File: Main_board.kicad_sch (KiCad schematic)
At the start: 199 parts, among them J1 USB_C_Receptacle_USB2.0_14P, J2 Conn_02x03_Odd_Even, SW1 SW_Push, SW10 SW_Push, SW11 SW_Push, SW12 SW_Push, SW13 SW_Push, SW14 SW_Push, SW15 SW_Push, SW16 SW_Push, SW17 SW_Push, SW18 SW_Push, SW19 SW_Push, SW2 SW_Push, SW20 SW_Push, SW21 SW_Push, SW22 SW_Push, SW23 SW_Push, SW24 SW_Push, SW25 SW_Push, SW26 SW_Push, SW27 SW_Push, SW28 SW_Push, SW29 SW_Push, SW3 SW_Push, SW30 SW_Push, SW31 SW_Push, SW32 SW_Push, SW33 SW_Push, SW34 SW_Push, SW35 SW_Push, SW36 SW_Push, SW37 SW_Push, SW38 SW_Push, SW39 SW_Push, SW4 SW_Push, SW40 SW_Push, SW41 SW_Push, SW42 SW_Push, SW43 SW_Push, SW44 SW_Push, SW45 SW_Push, SW46 SW_Push, SW47 SW_Push, SW48 SW_Push, SW49 SW_Push, SW5 SW_Push, SW50 SW_Push, SW51 SW_Push, SW52 SW_Push, SW53 SW_Push, SW54 SW_Push, SW55 SW_Push, SW56 SW_Push, SW57 SW_Push, SW58 SW_Push, SW59 SW_Push, SW6 SW_Push, SW60 SW_Push, SW61 SW_Push, SW62 SW_Push, SW63 SW_Push, SW64 SW_Push, SW65 SW_Push, SW66 SW_Push, SW67 SW_Push, SW68 SW_Push, SW69 SW_Push, SW7 SW_Push, SW70 SW_Push, SW71 SW_Push, SW72 SW_Push, SW73 SW_Push, SW74 SW_Push, SW75 SW_Push, SW76 SW_Push, SW77 SW_Push, SW78 SW_Push, SW79 SW_Push, SW8 SW_Push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

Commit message: Finished the main board's design
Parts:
- added D104, D105, D106, D107, D108, D109, D110, D111, D112, D113, D114, D115, D116, D117, D118, D119, D120, D121, D122, D123, D124, D125, D126, D127, D128, D129, D130, D131, D132, D133, D134, D135, D136, D137, D138, D139, D140, D141, D142, D143, D144, D145, D146, D147, D148, D149, D150, D151, D152, D153, D154, D155, D156, D157, D158, D159, D160, D161, D162, D163, D164, D165, D166, D167, D168, D169, D170, D171, D172, D173, D174, D175, D176, D177, D178, D179, D180, D181, D182, D183, D184, D185: SK6805, LED_SMD:LED_SK6805_PLCC4_2.4x2.7mm_P1.3mm, symbol LED:SK6805
- added H1, H2, H3, H4: MountingHole, MountingHole:MountingHole_2.2mm_M2, symbol Mechanical:MountingHole
- added U11: MT3608_Module, Footprints:MT3608-Module, symbol Custom Symbols:MT3608_Module
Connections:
- net GND: now also D104.2 (VSS), D105.2 (VSS), D106.2 (VSS), D107.2 (VSS), D108.2 (VSS), D109.2 (VSS), D110.2 (VSS), D111.2 (VSS), D112.2 (VSS), D113.2 (VSS), D114.2 (VSS), D115.2 (VSS), D116.2 (VSS), D117.2 (VSS), D118.2 (VSS), D119.2 (VSS), D120.2 (VSS), D121.2 (VSS), D122.2 (VSS), D123.2 (VSS), D124.2 (VSS), D125.2 (VSS), D126.2 (VSS), D127.2 (VSS), D128.2 (VSS), D129.2 (VSS), D130.2 (VSS), D131.2 (VSS), D132.2 (VSS), D133.2 (VSS), D134.2 (VSS), D135.2 (VSS), D136.2 (VSS), D137.2 (VSS), D138.2 (VSS), D139.2 (VSS), D140.2 (VSS), D141.2 (VSS), D142.2 (VSS), D143.2 (VSS), D144.2 (VSS), D145.2 (VSS), D146.2 (VSS), D147.2 (VSS), D148.2 (VSS), D149.2 (VSS), D150.2 (VSS), D151.2 (VSS), D152.2 (VSS), D153.2 (VSS), D154.2 (VSS), D155.2 (VSS), D156.2 (VSS), D157.2 (VSS), D158.2 (VSS), D159.2 (VSS), D160.2 (VSS), D161.2 (VSS), D162.2 (VSS), D163.2 (VSS), D164.2 (VSS), D165.2 (VSS), D166.2 (VSS), D167.2 (VSS), D168.2 (VSS), D169.2 (VSS), D170.2 (VSS), D171.2 (VSS), D172.2 (VSS), D173.2 (VSS), D174.2 (VSS), D175.2 (VSS), D176.2 (VSS), D177.2 (VSS), D178.2 (VSS), D179.2 (VSS), D180.2 (VSS), D181.2 (VSS), D182.2 (VSS), D183.2 (VSS), D184.2 (VSS), D185.2 (VSS), U11.2 (VIN-), U11.4 (VOUT-)
- net M3V3: now also C2.1, U3.30 (VDDH), U3.32 (VBUS), U11.1 (VIN+)
- net MBT_PIN: now also U3.11 (P0.02)
- net MFLT: now also U3.7 (P1.14); no longer U3.24 (P0.08)
- net MID1: now also U3.25 (P1.08); no longer U3.61 (P1.01)
- net MID2: now also U3.20 (P0.04)
- net MID3: now also U3.24 (P0.08); no longer U3.60 (P1.03)
- net MID4: now also U3.27 (P0.11); no longer U3.56 (P1.04)
- net MINT1: now also U3.23 (P0.07); no longer U3.59 (P1.05)
- net MINT2: now also U3.18 (P0.01); no longer U3.57 (P1.06)
- net MINT3: now also U3.26 (P1.09); no longer U3.58 (P1.07)
- net MINT4: now also U3.22 (P0.06); no longer U3.25 (P1.08)
- net MRESET: now also U3.5 (P1.12)
- net MSCL: now also U3.19 (P0.26)
- net MSDA: now also U3.21 (P0.05); no longer U3.26 (P1.09)
- net MUSB_DET: now also U3.3 (P1.10)
- net MVB_EN: now also U3.13 (P0.28); no longer U3.22 (P0.06)
- net VDD: now also D104.4 (VDD), D105.4 (VDD), D106.4 (VDD), D107.4 (VDD), D108.4 (VDD), D109.4 (VDD), D110.4 (VDD), D111.4 (VDD), D112.4 (VDD), D113.4 (VDD), D114.4 (VDD), D115.4 (VDD), D116.4 (VDD), D117.4 (VDD), D118.4 (VDD), D119.4 (VDD), D120.4 (VDD), D121.4 (VDD), D122.4 (VDD), D123.4 (VDD), D124.4 (VDD), D125.4 (VDD), D126.4 (VDD), D127.4 (VDD), D128.4 (VDD), D129.4 (VDD), D130.4 (VDD), D131.4 (VDD), D132.4 (VDD), D133.4 (VDD), D134.4 (VDD), D135.4 (VDD), D136.4 (VDD), D137.4 (VDD), D138.4 (VDD), D139.4 (VDD), D140.4 (VDD), D141.4 (VDD), D142.4 (VDD), D143.4 (VDD), D144.4 (VDD), D145.4 (VDD), D146.4 (VDD), D147.4 (VDD), D148.4 (VDD), D149.4 (VDD), D150.4 (VDD), D151.4 (VDD), D152.4 (VDD), D153.4 (VDD), D154.4 (VDD), D155.4 (VDD), D156.4 (VDD), D157.4 (VDD), D158.4 (VDD), D159.4 (VDD), D160.4 (VDD), D161.4 (VDD), D162.4 (VDD), D163.4 (VDD), D164.4 (VDD), D165.4 (VDD), D166.4 (VDD), D167.4 (VDD), D168.4 (VDD), D169.4 (VDD), D170.4 (VDD), D171.4 (VDD), D172.4 (VDD), D173.4 (VDD), D174.4 (VDD), D175.4 (VDD), D176.4 (VDD), D177.4 (VDD), D178.4 (VDD), D179.4 (VDD), D180.4 (VDD), D181.4 (VDD), D182.4 (VDD), D183.4 (VDD), D184.4 (VDD), D185.4 (VDD), U11.3 (VOUT+); no longer C2.1, C7.1, J1.A4 (VBUS), J1.A9 (VBUS), J1.B4 (VBUS), J1.B9 (VBUS), R12.2, U2.1 (VBUS), U2.8 (VBUS), U3.30 (VDDH), U3.32 (VBUS), U5.4 (V_{DD})
- net MVBUS_SW renamed MV_SW
- new net: D168.1 (DOUT), D169.3 (DIN)
- new net: D167.1 (DOUT), D168.3 (DIN)
- new net: D165.1 (DOUT), D166.3 (DIN)
- new net: D164.1 (DOUT), D165.3 (DIN)
- new net: D142.1 (DOUT), D143.3 (DIN)
- new net: D141.1 (DOUT), D142.3 (DIN)
- new net: D138.1 (DOUT), D139.3 (DIN)
- new net: D137.1 (DOUT), D138.3 (DIN)
- new net: D153.3 (DIN), D154.1 (DOUT)
- new net: D154.3 (DIN), D155.1 (DOUT)
- new net: D112.1 (DOUT), D113.3 (DIN)
- new net: D111.1 (DOUT), D112.3 (DIN)
- new net: D180.3 (DIN), D181.1 (DOUT)
- new net: D181.3 (DIN), D182.1 (DOUT)
- new net: D131.3 (DIN), D132.1 (DOUT)
- new net: D117.1 (DOUT), D132.3 (DIN)
- new net: D130.3 (DIN), D131.1 (DOUT)
- new net: D127.3 (DIN), D128.1 (DOUT)
- new net: D128.3 (DIN), D129.1 (DOUT)
- new net: D105.1 (DOUT), D106.3 (DIN)
- new net: D104.1 (DOUT), D105.3 (DIN)
- new net: D120.3 (DIN), D121.1 (DOUT)
- new net: D121.3 (DIN), D122.1 (DOUT)
- new net: D177.3 (DIN), D178.1 (DOUT)
- new net: D178.3 (DIN), D179.1 (DOUT)
- new net: D139.1 (DOUT), D140.3 (DIN)
- new net: D172.1 (DOUT), D173.3 (DIN)
- new net: D171.1 (DOUT), D172.3 (DIN)
- new net: D143.1 (DOUT), D144.3 (DIN)
- new net: D118.3 (DIN), D119.1 (DOUT)
- new net: D119.3 (DIN), D120.1 (DOUT)
- new net: D151.3 (DIN), D152.1 (DOUT)
- new net: D152.3 (DIN), D153.1 (DOUT)
- new net: D115.1 (DOUT), D116.3 (DIN)
- new net: D114.1 (DOUT), D115.3 (DIN)
- new net: D106.1 (DOUT), D107.3 (DIN)
- new net: D134.1 (DOUT), D135.3 (DIN)
- new net: D133.1 (DOUT), D134.3 (DIN)
- new net: D150.3 (DIN), D151.1 (DOUT)
- new net: D116.1 (DOUT), D117.3 (DIN)
- new net: D184.3 (DIN), D185.1 (DOUT)
- new net: D174.1 (DOUT), D185.3 (DIN)
- new net: D166.1 (DOUT), D167.3 (DIN)
- new net: D129.3 (DIN), D130.1 (DOUT)
- new net: D122.3 (DIN), D123.1 (DOUT)
- new net: D118.1 (DOUT), D133.3 (DIN)
- new net: D147.1 (DOUT), D161.3 (DIN)
- new net: D146.1 (DOUT), D147.3 (DIN)
- new net: D162.1 (DOUT), D163.3 (DIN)
- new net: D148.1 (DOUT), D162.3 (DIN)
- new net: D173.1 (DOUT), D174.3 (DIN)
- new net: D183.3 (DIN), D184.1 (DOUT)
- new net: D109.1 (DOUT), D110.3 (DIN)
- new net: D108.1 (DOUT), D109.3 (DIN)
- new net: D155.3 (DIN), D156.1 (DOUT)
- new net: D156.3 (DIN), D157.1 (DOUT)
- new net: D163.1 (DOUT), D164.3 (DIN)
- new net: D157.3 (DIN), D158.1 (DOUT)
- new net: D158.3 (DIN), D159.1 (DOUT)
- new net: D140.1 (DOUT), D141.3 (DIN)
- new net: D148.3 (DIN), D149.1 (DOUT)
- new net: D136.1 (DOUT), D137.3 (DIN)
- new net: D135.1 (DOUT), D136.3 (DIN)
- new net: D107.1 (DOUT), D108.3 (DIN)
- new net: D110.1 (DOUT), D111.3 (DIN)
- new net: D113.1 (DOUT), D114.3 (DIN)
- new net: D182.3 (DIN), D183.1 (DOUT)
- new net: D179.3 (DIN), D180.1 (DOUT)
- new net: D149.3 (DIN), D150.1 (DOUT)
- new net: D145.1 (DOUT), D146.3 (DIN)
- new net: D175.3 (DIN), D176.1 (DOUT)
- new net: D176.3 (DIN), D177.1 (DOUT)
- new net: D170.1 (DOUT), D171.3 (DIN)
- new net: D123.3 (DIN), D124.1 (DOUT)
- new net: D124.3 (DIN), D125.1 (DOUT)
- new net: D169.1 (DOUT), D170.3 (DIN)
- new net: D126.3 (DIN), D127.1 (DOUT)
- new net: D144.1 (DOUT), D145.3 (DIN)
- new net: D160.3 (DIN), D161.1 (DOUT)
- new net: D125.3 (DIN), D126.1 (DOUT)
- new net: D159.3 (DIN), D160.1 (DOUT)
- new net MLEDs: D104.3 (DIN), U3.56 (P1.04)
- new net MVBUS: C7.1, J1.A4 (VBUS), J1.A9 (VBUS), J1.B4 (VBUS), J1.B9 (VBUS), R12.2, U2.1 (VBUS), U2.8 (VBUS), U5.4 (V_{DD})
- no-connect marks 14 -> 18
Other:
- moved on the sheet: C1, C2, D83, R10, R5, R8, R9, U3

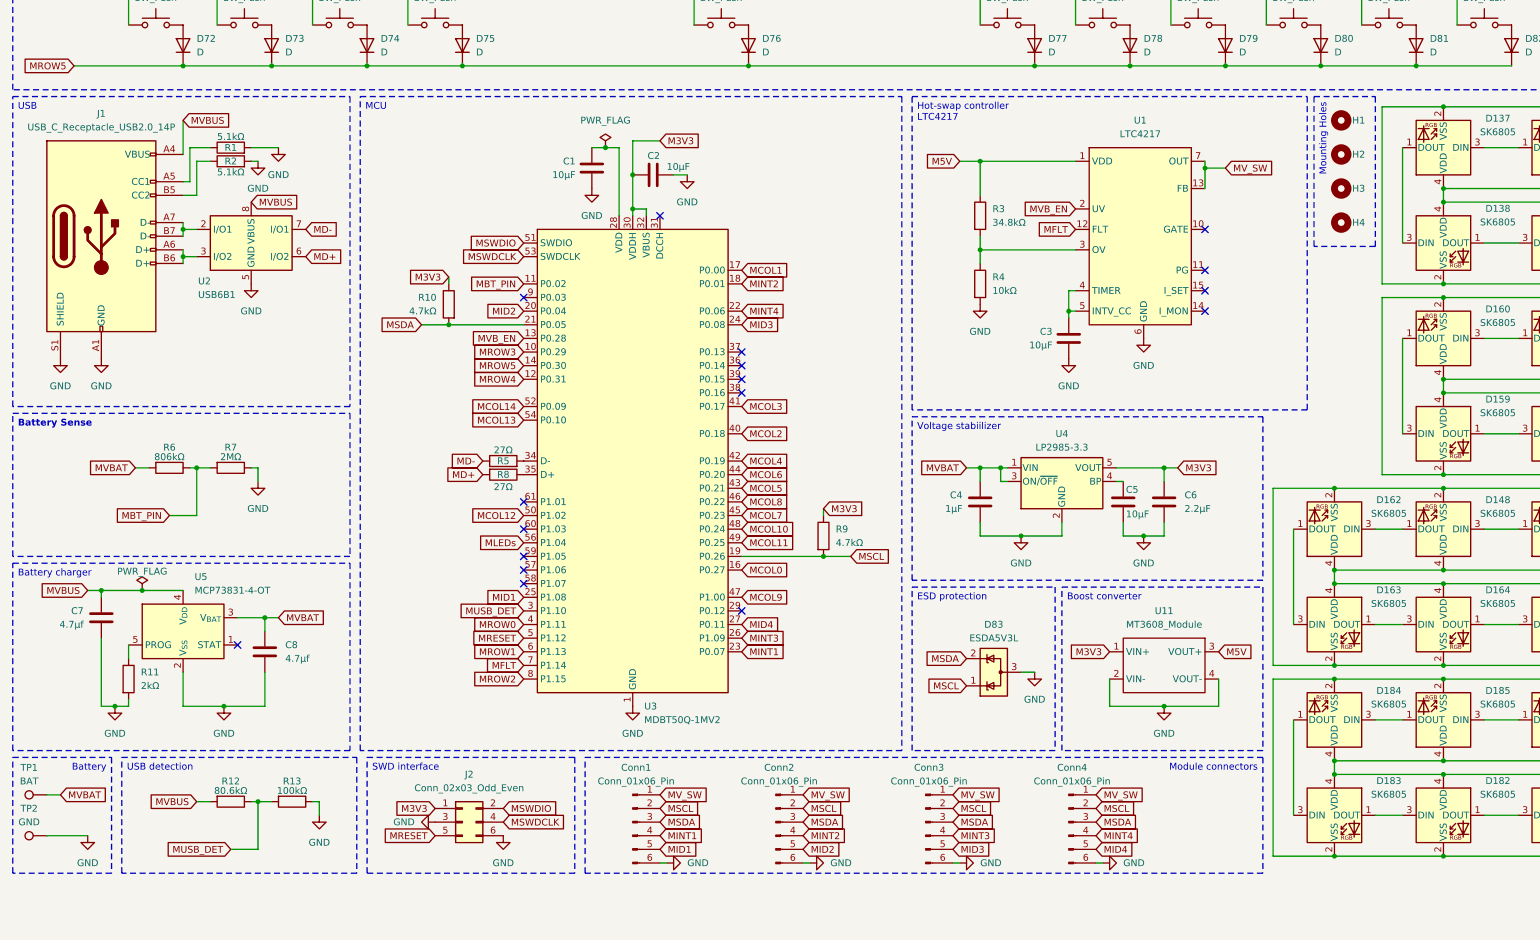
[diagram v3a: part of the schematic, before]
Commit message: Reduced the main keyboard's profile
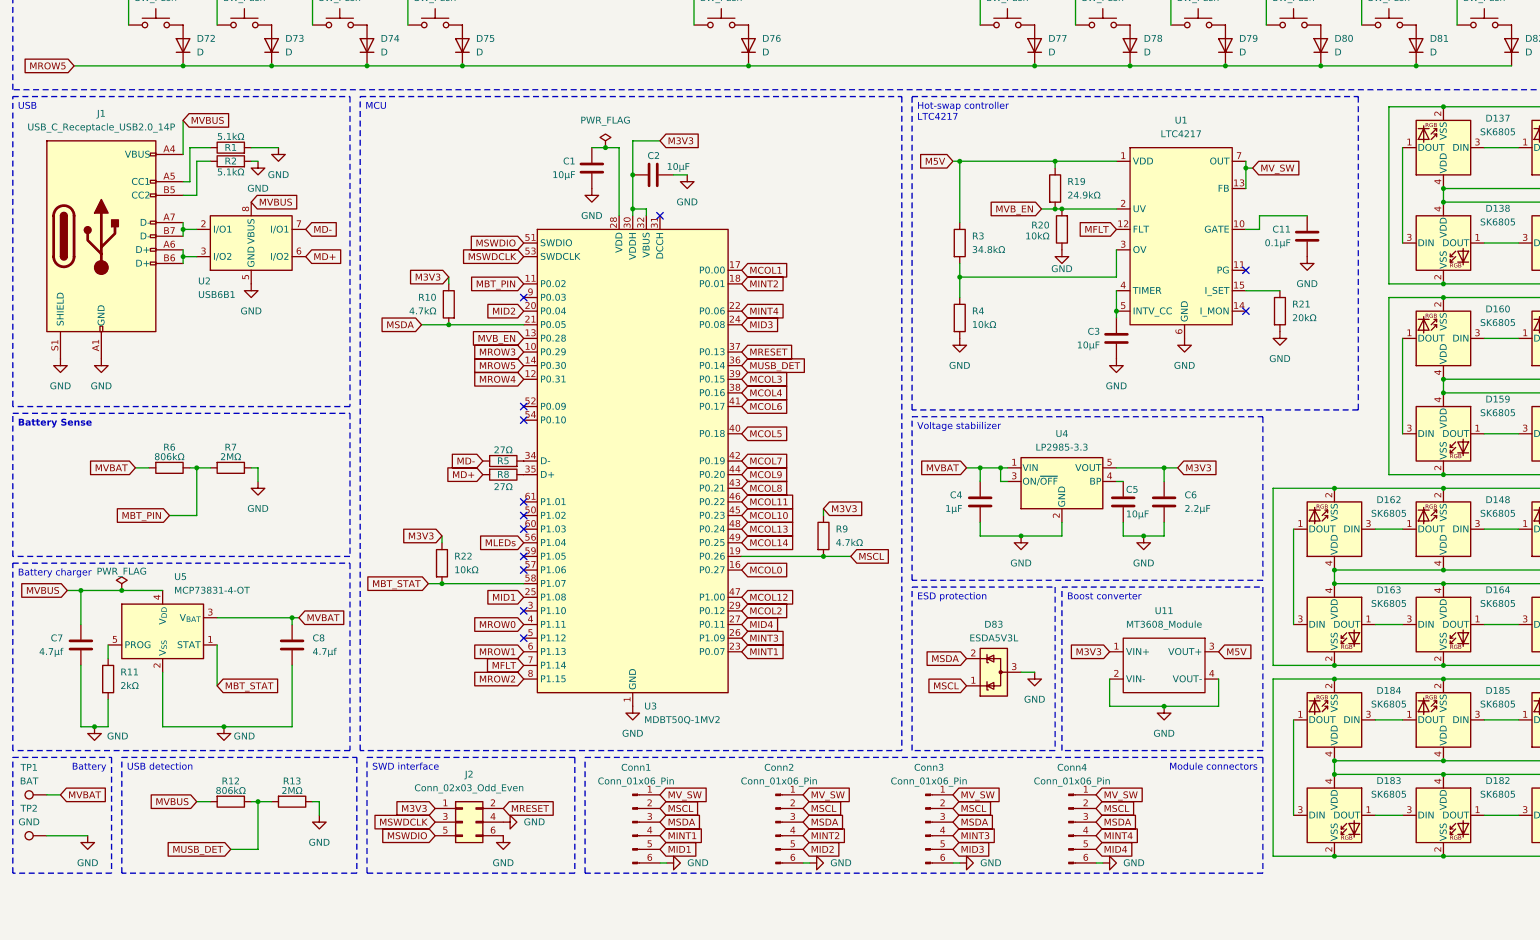
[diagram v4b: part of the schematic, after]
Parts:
- removed H1, H2, H3, H4: MountingHole, MountingHole:MountingHole_2.2mm_M2, symbol Mechanical:MountingHole
- added C11: 0.1µF, Capacitor_SMD:C_0805_2012Metric, symbol Device:C
- added R19: 24.9kΩ, Resistor_SMD:R_0805_2012Metric, symbol Device:R
- added R20, R22: 10kΩ, Resistor_SMD:R_0805_2012Metric, symbol Device:R
- added R21: 20kΩ, Resistor_SMD:R_0805_2012Metric, symbol Device:R
- R12: value 80.6kΩ -> 806kΩ
- R13: value 100kΩ -> 2MΩ
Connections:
- net GND: now also J2.4 (Pin_4), C11.2, R20.1, R21.2; no longer J2.3 (Pin_3)
- net M3V3: now also R22.1
- net MCOL10: now also U3.45 (P0.23); no longer U3.48 (P0.24)
- net MCOL11: now also U3.46 (P0.22); no longer U3.49 (P0.25)
- net MCOL12: now also U3.47 (P1.00); no longer U3.50 (P1.02)
- net MCOL13: now also U3.48 (P0.24); no longer U3.54 (P0.10)
- net MCOL14: now also U3.49 (P0.25); no longer U3.52 (P0.09)
- net MCOL2: now also U3.29 (P0.12); no longer U3.40 (P0.18)
- net MCOL3: now also U3.39 (P0.15); no longer U3.41 (P0.17)
- net MCOL4: now also U3.38 (P0.16); no longer U3.42 (P0.19)
- net MCOL5: now also U3.40 (P0.18); no longer U3.43 (P0.21)
- net MCOL6: now also U3.41 (P0.17); no longer U3.44 (P0.20)
- net MCOL7: now also U3.42 (P0.19); no longer U3.45 (P0.23)
- net MCOL8: now also U3.43 (P0.21); no longer U3.46 (P0.22)
- net MCOL9: now also U3.44 (P0.20); no longer U3.47 (P1.00)
- net MRESET: now also J2.2 (Pin_2), U3.37 (P0.13); no longer J2.5 (Pin_5), U3.5 (P1.12)
- net MSWDCLK: now also J2.3 (Pin_3); no longer J2.4 (Pin_4)
- net MSWDIO: now also J2.5 (Pin_5); no longer J2.2 (Pin_2)
- net MUSB_DET: now also U3.36 (P0.14); no longer U3.3 (P1.10)
- net MVB_EN: now also R19.2, R20.2
- net VDD: now also R19.1
- net at U1.10 (GATE): now also C11.1
- net at U1.15 (I_SET): now also R21.1
- net MBT_STAT: now reaches U3.58 (P1.07)
- net MBT_STAT: now also U5.1 (STAT), R22.2
- no-connect marks 18 -> 14
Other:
- moved on the sheet: C3, C7, C8, R11, R3, R4, U1, U5

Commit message: fix issues with LTC4217
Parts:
- U1: footprint LTC4217IDHC_PBF:DFN-16_DHC -> footprints:DFN-16_DHC_LIT
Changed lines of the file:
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@@
 			)
 		)
-		(property "Footprint" "LTC4217IDHC_PBF:DFN-16_DHC"
+		(property "Footprint" "footprints:DFN-16_DHC_LIT"
 			(at 233.68 147.32 0)
 			(effects
